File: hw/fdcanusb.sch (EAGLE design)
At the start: 37 parts, among them J1 MF-CON-MICROUSB-RIGHT, J3 JST-ZH6SMT_VERT, M1 MOUNT, M2 MOUNT, M3 MOUNT, M4 MOUNT, U1 MF-REG-SOT235-3.3V-300mA, U2 USBLC6-2SC6, U3 TCAN334G, U4 TLP3317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

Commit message: Fix some housepart designations
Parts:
- R1, R2, R3, R4: HOUSEPART (none) -> YES
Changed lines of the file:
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@@
 <part name="D4" library="mfleds" deviceset="LED_SINGLE" device="-0603-RED" value="MF-LED-0603-RED"/>
 <part name="R1" library="mfpassives" deviceset="RESISTOR" device="_0603" value="220">
+<attribute name="HOUSEPART" value="YES"/>
 <attribute name="MPN" value="MF-RES-0603-220"/>
 </part>
 <part name="R2" library="mfpassives" deviceset="RESISTOR" device="_0603" value="220">
+<attribute name="HOUSEPART" value="YES"/>
 <attribute name="MPN" value="MF-RES-0603-220"/>
 </part>
 <part name="R3" library="mfpassives" deviceset="RESISTOR" device="_0603" value="220">
+<attribute name="HOUSEPART" value="YES"/>
 <attribute name="MPN" value="MF-RES-0603-220"/>
 </part>
 <part name="R4" library="mfpassives" deviceset="RESISTOR" device="_0603" value="220">
+<attribute name="HOUSEPART" value="YES"/>
 <attribute name="MPN" value="MF-RES-0603-220"/>
 </part>

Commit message: Fine silk placement
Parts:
- R6: HOUSEPART (none) -> YES
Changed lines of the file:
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@@
 <part name="+3V8" library="supply1" deviceset="+3V3" device=""/>
 <part name="R6" library="mfpassives" deviceset="RESISTOR" device="_0603" value="330">
+<attribute name="HOUSEPART" value="YES"/>
 <attribute name="MPN" value="MF-RES-0603-330"/>
 </part>

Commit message: Fix resistor footprint
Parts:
- R5: device mfpassives:RESISTOR_0805 -> mfpassives:RESISTOR_0603
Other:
- note added: "mjbots fdcanusb r2.5 (c) 2021 Josh Pieper, jpieper@mjbots.com Licensed under the Apache 2.0 License https://www.apache.org/licenses/LICENSE-2.0"
- note removed: "mjbots fdcanusb r2.4 (c) 2021 Josh Pieper, jpieper@mjbots.com Licensed under the Apache 2.0 License https://www.apache.org/licenses/LICENSE-2.0"
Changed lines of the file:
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@@
 <part name="GND12" library="supply1" deviceset="GND" device=""/>
 <part name="+3V7" library="supply1" deviceset="+3V3" device=""/>
-<part name="R5" library="mfpassives" deviceset="RESISTOR" device="_0805" value="120">
+<part name="R5" library="mfpassives" deviceset="RESISTOR" device="_0603" value="120">
 <attribute name="MF" value="YAGEO"/>
 <attribute name="MPN" value="RC0603FR-07120RL"/>
@@
 <wire x1="-5.08" y1="-63.5" x2="-5.08" y2="88.9" width="0.1524" layer="90"/>
 <text x="0" y="73.66" size="7.62" layer="90">MOUNTS / POWER</text>
-<text x="-5.08" y="93.98" size="3.81" layer="90">mjbots fdcanusb r2.4
+<text x="-5.08" y="93.98" size="3.81" layer="90">mjbots fdcanusb r2.5
 (c) 2021 Josh Pieper, jpieper@mjbots.com
 Licensed under the Apache 2.0 License

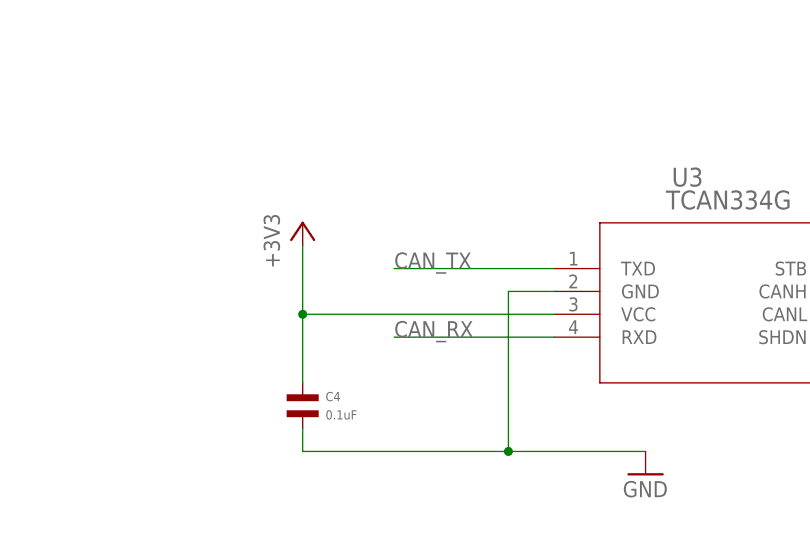
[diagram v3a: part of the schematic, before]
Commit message: SCHEMATIC ONLY work on more CAN transceiver variants
Update schematic, but not PCB, to accept the TCAN1057AEV in addition
to the 3.3V native variants.
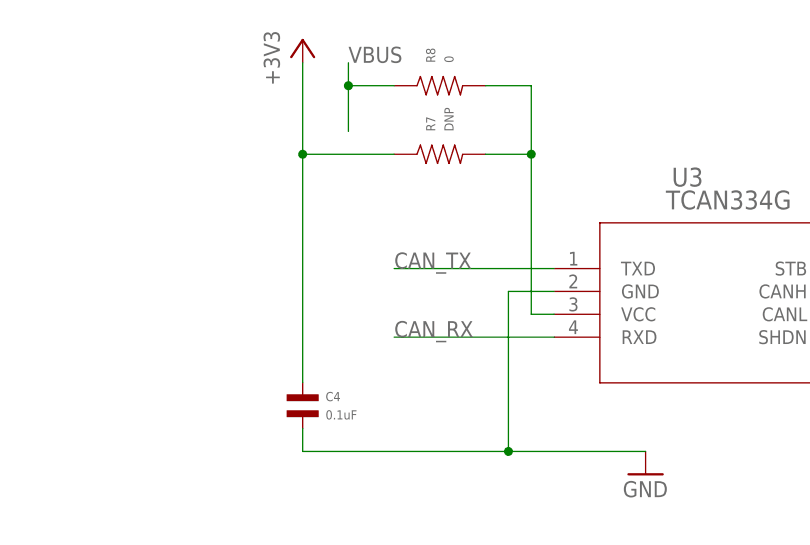
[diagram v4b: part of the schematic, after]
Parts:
- added R7: DNP, mfpassives:RESISTOR_0603
- added R8: 0, mfpassives:RESISTOR_0603
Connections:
- new net N$1: R7.P$2, R8.P$2, U3.VCC
- net +3V3: now also R7.P$1; no longer U3.VCC
- net VBUS: now also R8.P$1
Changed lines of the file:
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@@
 <attribute name="MPN" value="MF-RES-0603-330"/>
+</part>
+<part name="R7" library="mfpassives" deviceset="RESISTOR" device="_0603" value="DNP">
+<attribute name="HOUSEPART" value="YES"/>
+<attribute name="POPULATE" value="0"/>
+</part>
+<part name="R8" library="mfpassives" deviceset="RESISTOR" device="_0603" value="0">
+<attribute name="HOUSEPART" value="YES"/>
+<attribute name="MPN" value="MF-RES-0603-0"/>
 </part>
 </parts>
@@
 <attribute name="VALUE" x="162.56" y="-205.74" size="1.778" layer="96" rot="R90"/>
 </instance>
-<instance part="+3V5" gate="G$1" x="307.34" y="53.34" smashed="yes">
-<attribute name="VALUE" x="304.8" y="48.26" size="1.778" layer="96" rot="R90"/>
+<instance part="+3V5" gate="G$1" x="307.34" y="73.66" smashed="yes">
+<attribute name="VALUE" x="304.8" y="68.58" size="1.778" layer="96" rot="R90"/>
 </instance>
 <instance part="GND8" gate="1" x="109.22" y="-134.62" smashed="yes">
@@
 <attribute name="NAME" x="355.6" y="-18.796" size="1.016" layer="95" font="vector" align="top-left"/>
 <attribute name="VALUE" x="355.6" y="-21.844" size="1.016" layer="96" font="vector"/>
+</instance>
+<instance part="R7" gate="G$1" x="322.58" y="60.96" smashed="yes" rot="R90">
+<attribute name="NAME" x="321.056" y="63.5" size="1.016" layer="95" font="vector" rot="R90" align="top-left"/>
+<attribute name="VALUE" x="324.104" y="63.5" size="1.016" layer="96" font="vector" rot="R90"/>
+</instance>
+<instance part="R8" gate="G$1" x="322.58" y="68.58" smashed="yes" rot="R90">
+<attribute name="NAME" x="321.056" y="71.12" size="1.016" layer="95" font="vector" rot="R90" align="top-left"/>
+<attribute name="VALUE" x="324.104" y="71.12" size="1.016" layer="96" font="vector" rot="R90"/>
 </instance>
 </instances>
@@
 <label x="157.48" y="33.02" size="1.778" layer="95"/>
 </segment>
+<segment>
+<wire x1="312.42" y1="71.12" x2="312.42" y2="68.58" width="0.1524" layer="91"/>
+<label x="312.42" y="71.12" size="1.778" layer="95"/>
+<pinref part="R8" gate="G$1" pin="P$1"/>
+<wire x1="312.42" y1="68.58" x2="312.42" y2="63.5" width="0.1524" layer="91"/>
+<wire x1="312.42" y1="68.58" x2="317.5" y2="68.58" width="0.1524" layer="91"/>
+<junction x="312.42" y="68.58"/>
+</segment>
 </net>
 <net name="USB_D_N" class="1">
@@
 <pinref part="+3V5" gate="G$1" pin="+3V3"/>
 <pinref part="C4" gate="G$1" pin="P$1"/>
-<wire x1="307.34" y1="50.8" x2="307.34" y2="43.18" width="0.1524" layer="91"/>
-<pinref part="U3" gate="G$1" pin="VCC"/>
-<wire x1="307.34" y1="43.18" x2="307.34" y2="35.56" width="0.1524" layer="91"/>
-<wire x1="335.28" y1="43.18" x2="307.34" y2="43.18" width="0.1524" layer="91"/>
-<junction x="307.34" y="43.18"/>
+<wire x1="307.34" y1="71.12" x2="307.34" y2="60.96" width="0.1524" layer="91"/>
+<pinref part="R7" gate="G$1" pin="P$1"/>
+<wire x1="307.34" y1="60.96" x2="307.34" y2="35.56" width="0.1524" layer="91"/>
+<wire x1="307.34" y1="60.96" x2="317.5" y2="60.96" width="0.1524" layer="91"/>
+<junction x="307.34" y="60.96"/>
 </segment>
 <segment>
@@
 </segment>
 </net>
+<net name="N$1" class="0">
+<segment>
+<pinref part="U3" gate="G$1" pin="VCC"/>
+<wire x1="335.28" y1="43.18" x2="332.74" y2="43.18" width="0.1524" layer="91"/>
+<wire x1="332.74" y1="43.18" x2="332.74" y2="60.96" width="0.1524" layer="91"/>
+<pinref part="R7" gate="G$1" pin="P$2"/>
+<wire x1="332.74" y1="60.96" x2="327.66" y2="60.96" width="0.1524" layer="91"/>
+<wire x1="332.74" y1="60.96" x2="332.74" y2="68.58" width="0.1524" layer="91"/>
+<junction x="332.74" y="60.96"/>
+<pinref part="R8" gate="G$1" pin="P$2"/>
+<wire x1="332.74" y1="68.58" x2="327.66" y2="68.58" width="0.1524" layer="91"/>
+</segment>
+</net>

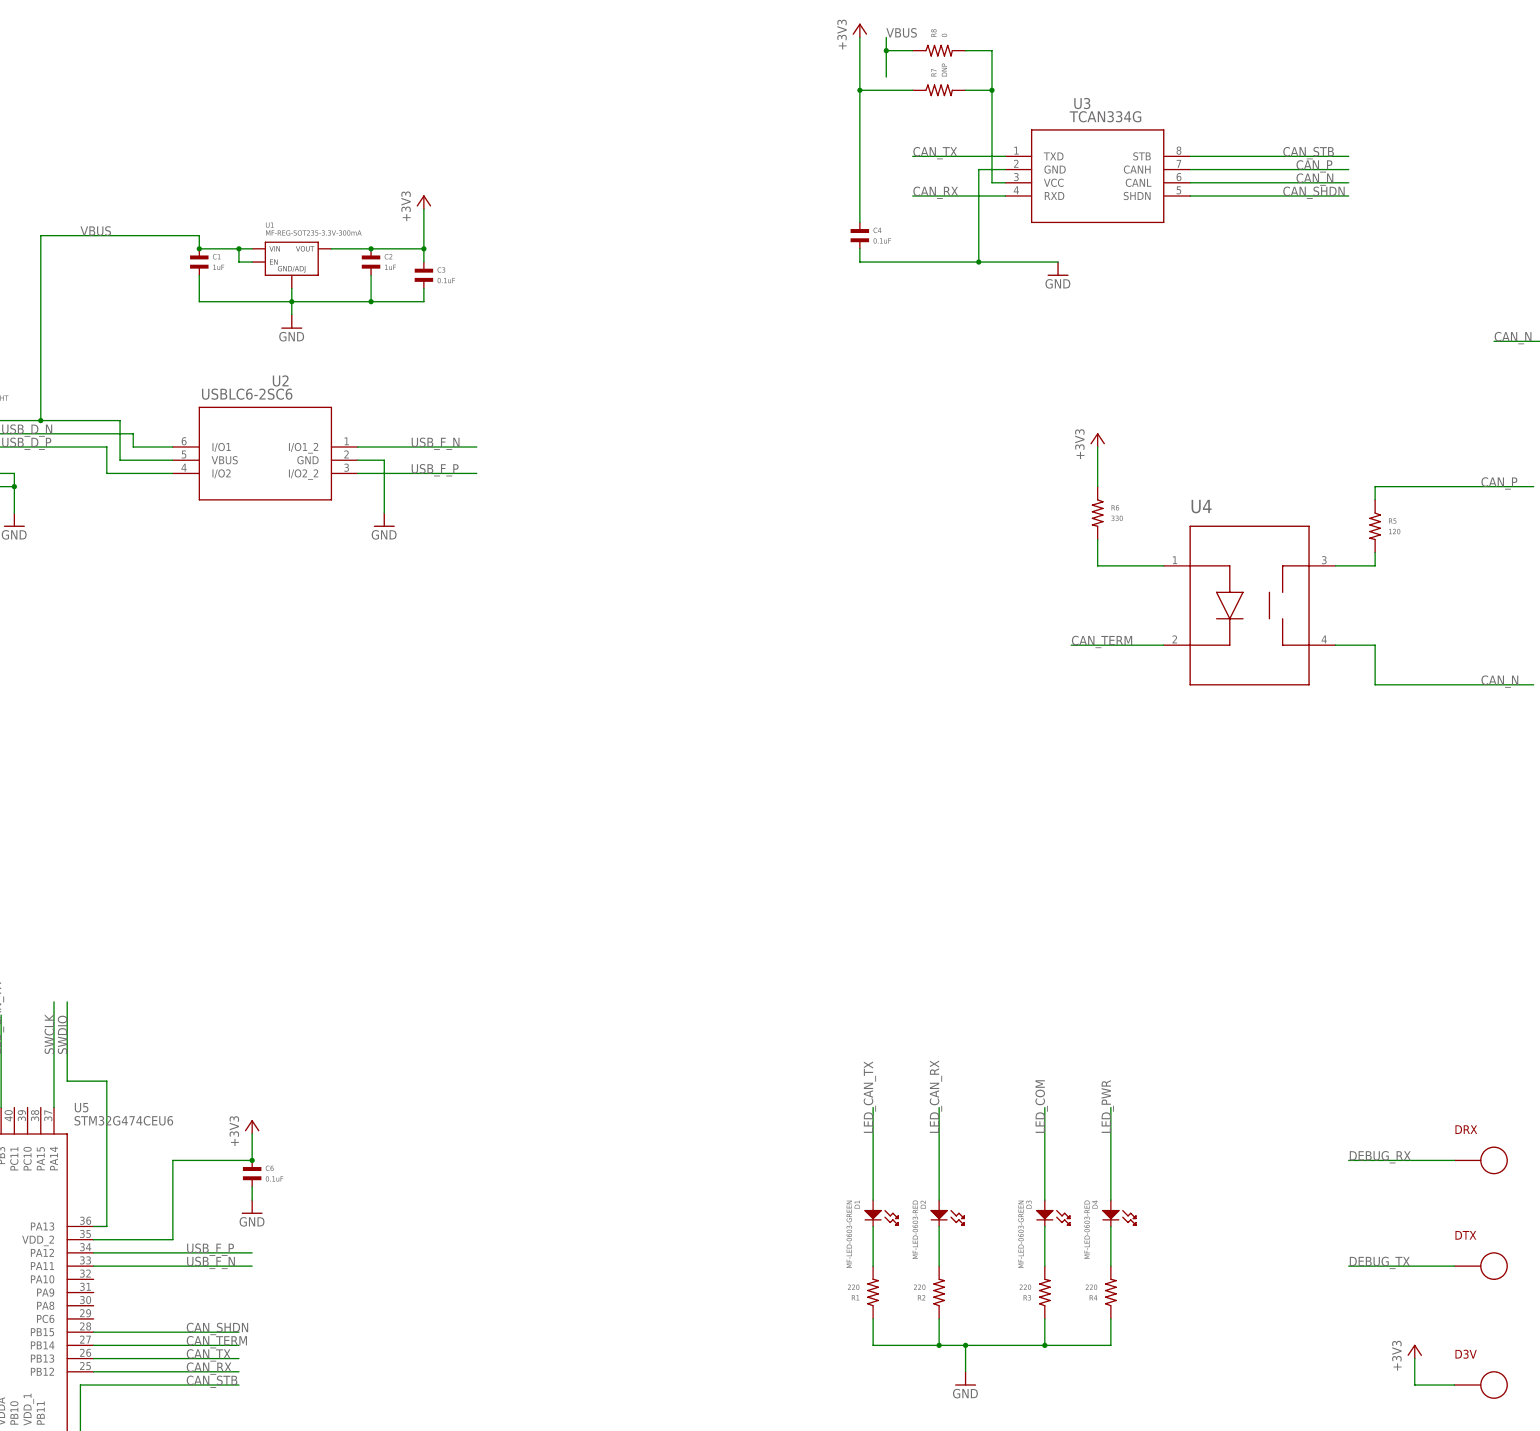
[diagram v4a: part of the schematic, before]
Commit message: Nominally complete fdcanusb w/ support for all known SOIC8/SOT8 CAN
* This will work with all the 3.3V and 5V 8 pin parts I know of with
  no more than different resistor populations.
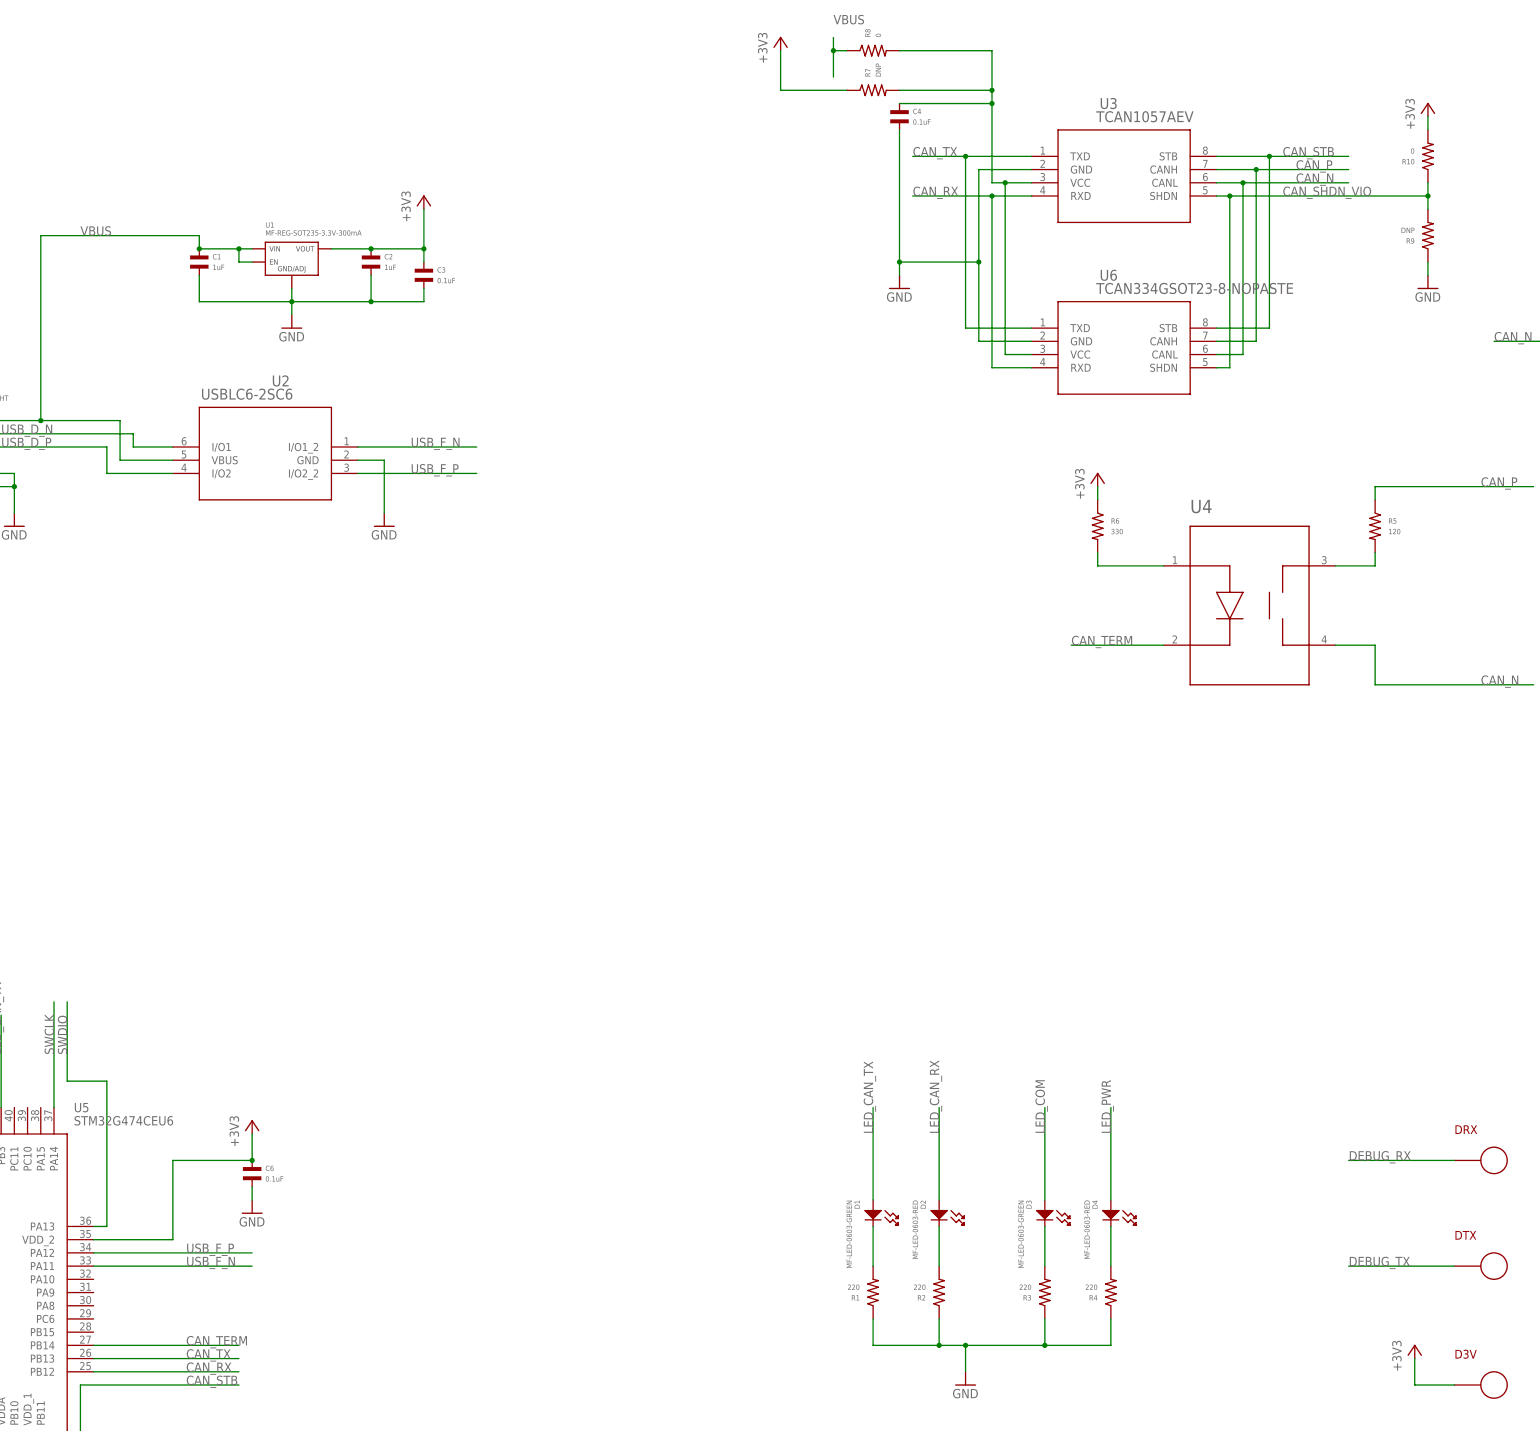
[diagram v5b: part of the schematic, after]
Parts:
- added R10: 0, mfpassives:RESISTOR_0603
- added R9: DNP, mfpassives:RESISTOR_0603
- added U6: TCAN334GSOT23-8-NOPASTE, controller:TCAN334GSOT23-8-NOPASTE
- U3: value TCAN334G -> TCAN1057AEV; MPN TCAN330GDR -> TCAN1057AEVDRQ1
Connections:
- removed net CAN_SHDN: U3.SHDN, U5.PB15
- new net CAN_SHDN_VIO: R10.P$1, R9.P$2, U3.SHDN, U6.SHDN
- net +3V3: now also R10.P$2; no longer C4.P$1
- net CAN_N: now also U6.CANL
- net CAN_P: now also U6.CANH
- net CAN_RX: now also U6.RXD
- net CAN_STB: now also U6.STB
- net CAN_TX: now also U6.TXD
- net GND: now also R9.P$1, U6.GND
- net N$1: now also C4.P$1, U6.VCC
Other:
- note added: "POPULATE RESISTOR ACCORDING TO CAN VCC REQUIREMENT"
- moved on the sheet: C4, R6, R7, R8, U3

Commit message: More silk tweaks
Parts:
- R5: value 120 -> 110; MPN RC0603FR-07120RL -> RC0603FR-07110RL
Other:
- note added: "mjbots fdcanusb r2.5 (c) 2022 Josh Pieper, jpieper@mjbots.com Licensed under the Apache 2.0 License https://www.apache.org/licenses/LICENSE-2.0"
- note removed: "mjbots fdcanusb r2.5 (c) 2021 Josh Pieper, jpieper@mjbots.com Licensed under the Apache 2.0 License https://www.apache.org/licenses/LICENSE-2.0"
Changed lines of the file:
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@@
 <part name="GND12" library="supply1" deviceset="GND" device=""/>
 <part name="+3V7" library="supply1" deviceset="+3V3" device=""/>
-<part name="R5" library="mfpassives" deviceset="RESISTOR" device="_0603" value="120">
+<part name="R5" library="mfpassives" deviceset="RESISTOR" device="_0603" value="110">
 <attribute name="MF" value="YAGEO"/>
-<attribute name="MPN" value="RC0603FR-07120RL"/>
+<attribute name="MPN" value="RC0603FR-07110RL"/>
 </part>
 <part name="U4" library="fdcanusb" deviceset="TLP3317" device="">
@@
 <text x="0" y="73.66" size="7.62" layer="90">MOUNTS / POWER</text>
 <text x="-5.08" y="93.98" size="3.81" layer="90">mjbots fdcanusb r2.5
-(c) 2021 Josh Pieper, jpieper@mjbots.com
+(c) 2022 Josh Pieper, jpieper@mjbots.com
 Licensed under the Apache 2.0 License
 https://www.apache.org/licenses/LICENSE-2.0</text>

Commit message: Add a decoupling cap on VIO
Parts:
- added C12: 0.1uF, mfpassives:CAPACITOR_NP_0603
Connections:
- net CAN_SHDN_VIO: now also C12.P$1
- net GND: now also C12.P$2
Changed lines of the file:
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@@
 <part name="GND13" library="supply1" deviceset="GND" device=""/>
 <part name="+3V9" library="supply1" deviceset="+3V3" device=""/>
+<part name="C12" library="mfpassives" deviceset="CAPACITOR_NP" device="_0603" value="0.1uF">
+<attribute name="HOUSEPART" value="YES"/>
+<attribute name="MPN" value="MF-CAP-0603-0.1uF"/>
+</part>
 </parts>
 <sheets>
@@
 <attribute name="VALUE" x="414.02" y="53.34" size="1.778" layer="96" rot="R90"/>
 </instance>
+<instance part="C12" gate="G$1" x="424.18" y="33.02" smashed="yes">
+<attribute name="NAME" x="426.72" y="34.544" size="1.016" layer="95" font="vector" align="top-left"/>
+<attribute name="VALUE" x="426.72" y="31.496" size="1.016" layer="96" font="vector"/>
+</instance>
 </instances>
 <busses>
@@
 <pinref part="GND13" gate="1" pin="GND"/>
 <wire x1="416.56" y1="27.94" x2="416.56" y2="25.4" width="0.1524" layer="91"/>
+<wire x1="416.56" y1="27.94" x2="424.18" y2="27.94" width="0.1524" layer="91"/>
+<junction x="416.56" y="27.94"/>
+<pinref part="C12" gate="G$1" pin="P$2"/>
+<wire x1="424.18" y1="27.94" x2="424.18" y2="30.48" width="0.1524" layer="91"/>
 </segment>
 </net>
@@
 <wire x1="416.56" y1="40.64" x2="416.56" y2="43.18" width="0.1524" layer="91"/>
 <junction x="416.56" y="40.64"/>
-</segment>
-</net>
+<wire x1="416.56" y1="40.64" x2="424.18" y2="40.64" width="0.1524" layer="91"/>
+<pinref part="C12" gate="G$1" pin="P$1"/>
+<wire x1="424.18" y1="40.64" x2="424.18" y2="35.56" width="0.1524" layer="91"/>
+</segment>
+</net>
